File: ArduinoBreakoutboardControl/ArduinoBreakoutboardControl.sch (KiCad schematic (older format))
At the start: 7 parts, among them M1 Conn_01x06_Male

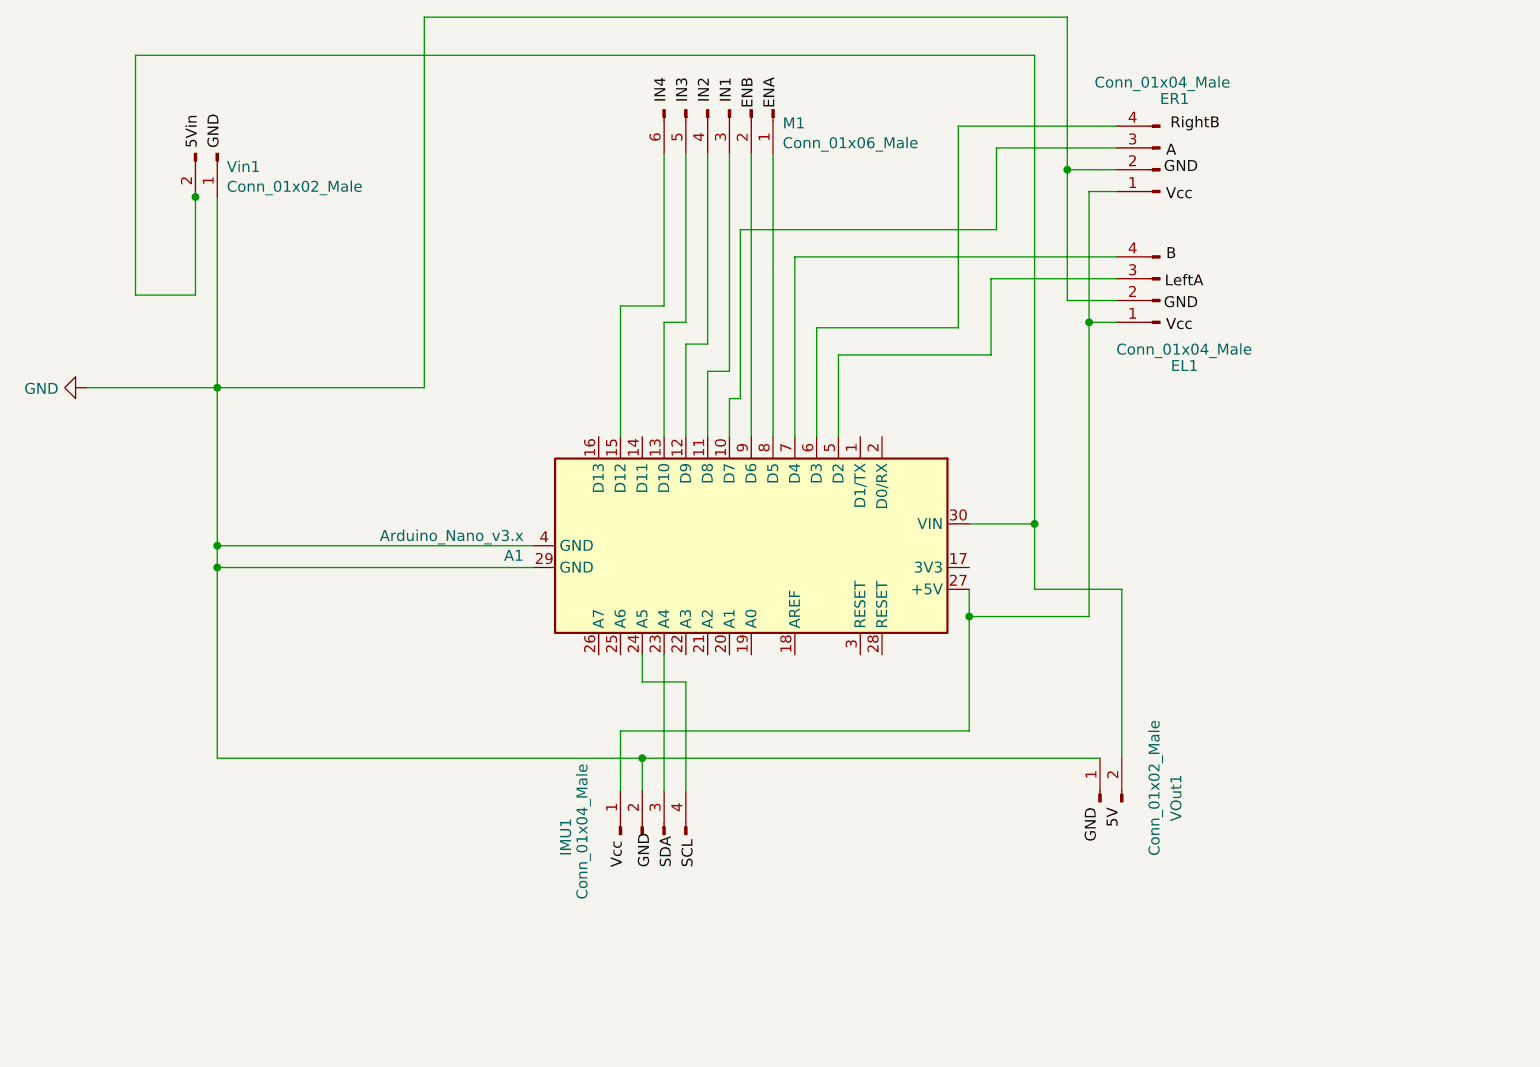
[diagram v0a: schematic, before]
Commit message: Added ground fill, fixed edge cuts, fixed 90 degree angles,
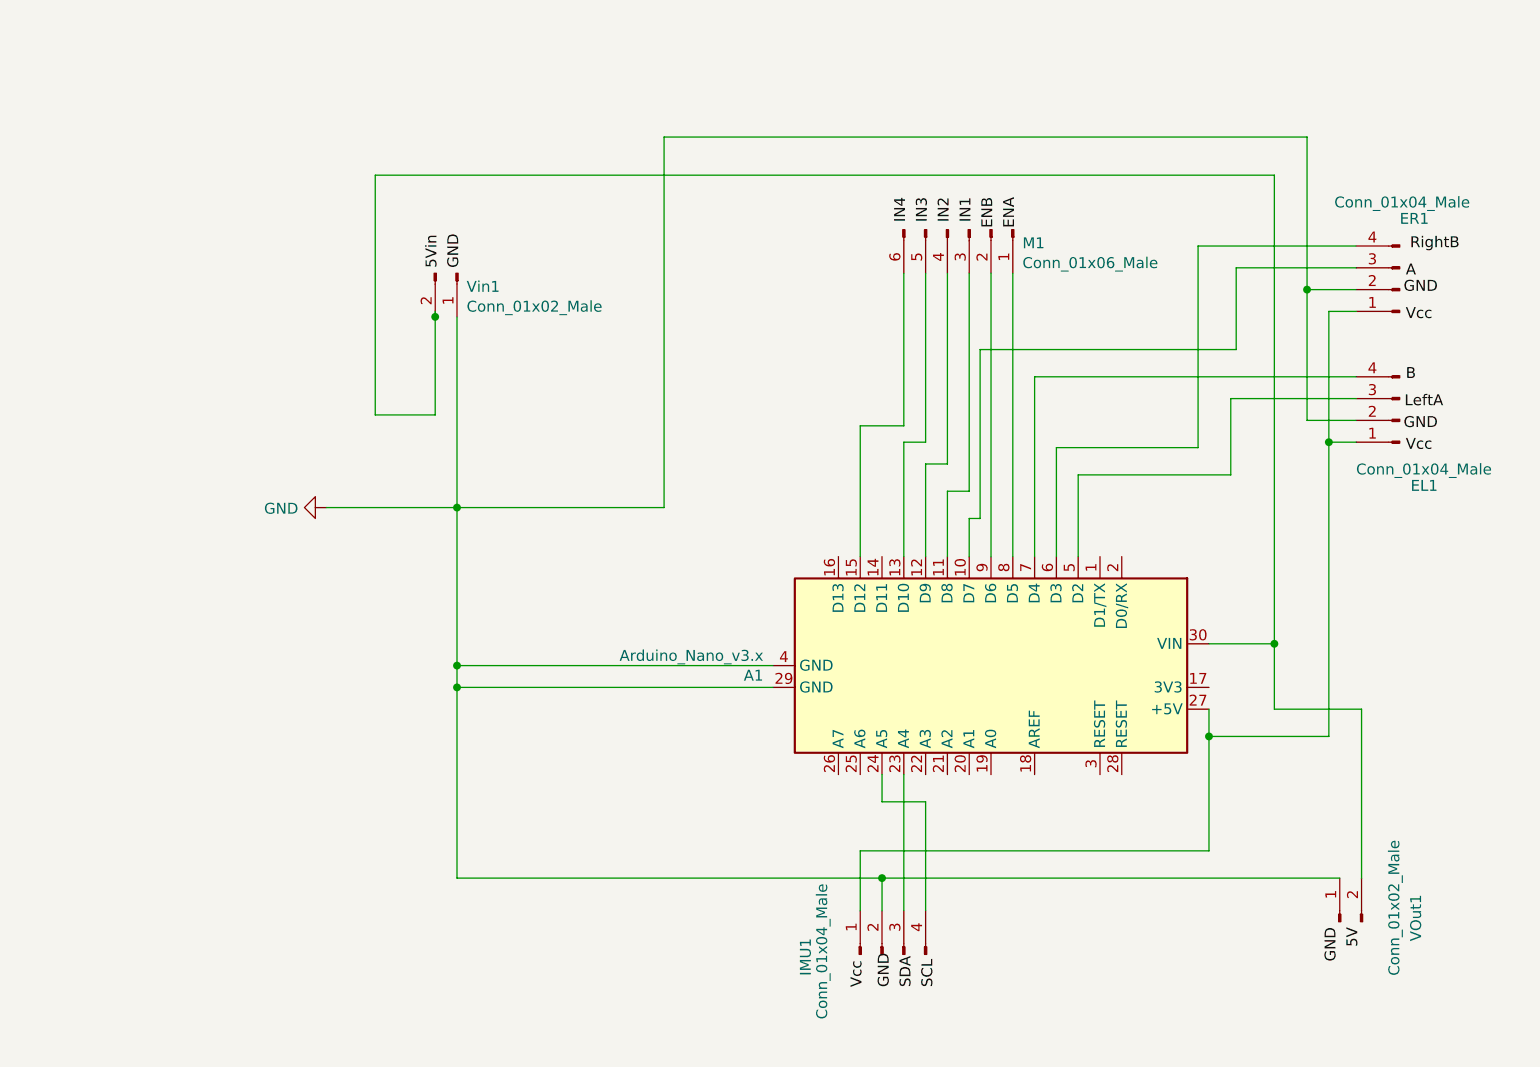
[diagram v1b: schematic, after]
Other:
- moved on the sheet: A1, EL1, ER1, IMU1, M1, VOut1, Vin1

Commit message: Changed DataSheets to datasheets
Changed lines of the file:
@@
 	8100 4950 8100 4175
-Wire Wire Line
-	3850 2375 3850 2825
-Connection ~ 3850 2375
 Wire Wire Line
 	3575 1725 7700 1725
@@
 Wire Wire Line
 	3850 2825 3575 2825
-Wire Wire Line
-	3850 2350 3850 2375
 Text Label 8100 5175 3    50   ~ 0
 5V
@@
 Text Label 6525 1825 3    50   ~ 0
 ENA
+Wire Wire Line
+	3850 2375 3850 2825
 $EndSCHEMATC
